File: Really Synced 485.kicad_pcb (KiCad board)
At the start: 2 copper layers, 34 parts, among them J1 CONN_02X04, J2 CONN_01X03, J3 CONN_01X03, J4 CONN_02X04, U1 CE_HEADER, U2 SN75179B, U3 SN65HVD82

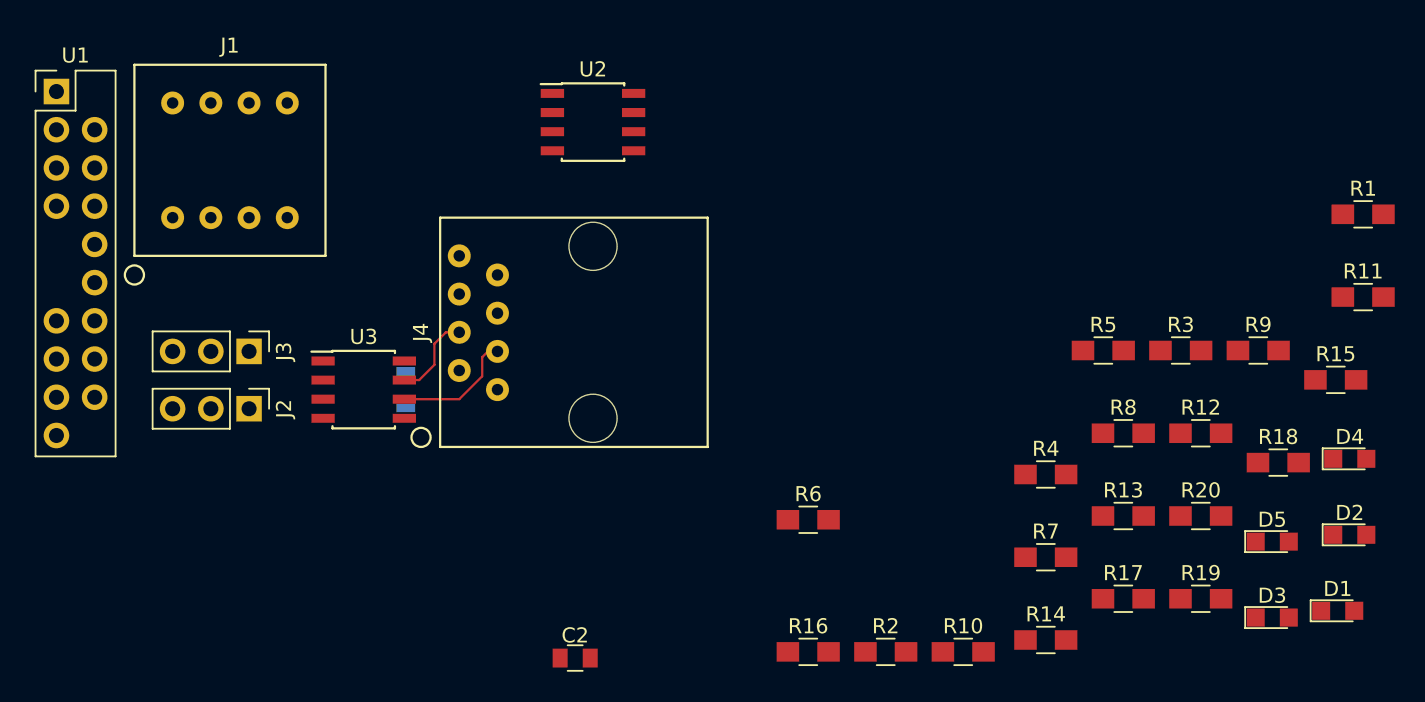
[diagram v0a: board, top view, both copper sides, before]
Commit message: Finished piano switch layout
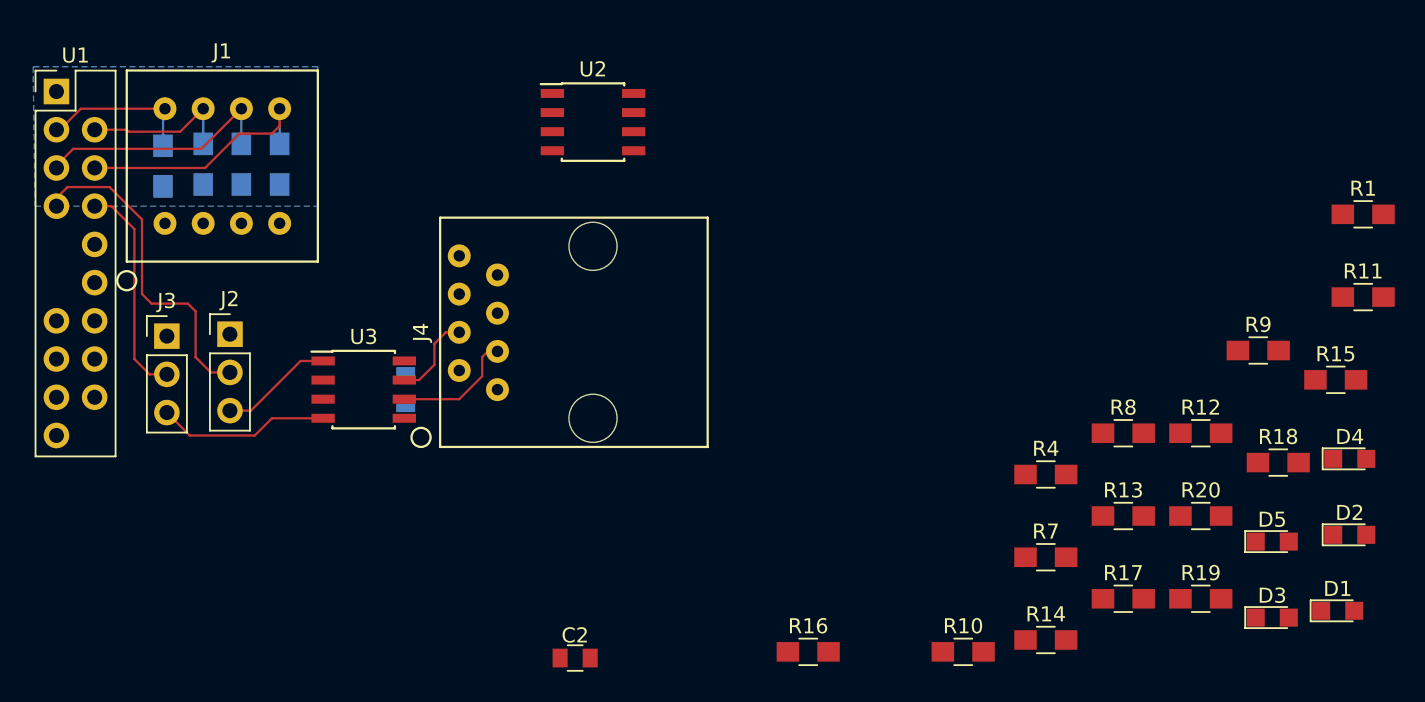
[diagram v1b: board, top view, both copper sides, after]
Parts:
- R2, R3, R5, R6: moved to B.Cu
- moved R3 66.1 mm to (132.8, 109.5), turned to 90 degrees
- moved R5 58.6 mm to (135.4, 109.5), turned to 90 degrees
- moved R2 57.9 mm to (130.2, 109.6), turned to 90 degrees
- moved R6 42.3 mm to (137.9, 109.5), turned to 90 degrees
- moved J3 5.55 mm to (130.4, 120.9), turned to 0 degrees
- moved J2 5.11 mm to (134.6, 120.8), turned to 0 degrees
- moved J1 0.64 mm to (134.1, 109.6)
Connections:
- net Net-(R2-Pad1) renamed /3.3V
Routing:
- net /RX: track 0.00 -> 22.2 mm
- net /ADDR3: track 0.00 -> 16.9 mm
- net /ADDR2: track 0.00 -> 16.3 mm
- net /TX: track 0.00 -> 14.5 mm
- net /TX_HALF: track 0.00 -> 11.5 mm
- net /ADDR0: track 0.00 -> 10.3 mm
- net /ADDR1: track 0.00 -> 10.2 mm
- net /RX_HALF: track 0.00 -> 7.56 mm
- added copper zone on B.Cu, net /3.3V

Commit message: Added ground plane and 5V power routing
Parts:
- C2, R1, R19, R20, R8, R9: moved to B.Cu
- moved D2 69.7 mm to (141.1, 118.7), turned to 90 degrees
- moved D1 68.4 mm to (143.0, 118.7), turned to 90 degrees
- moved D3 68.1 mm to (139.1, 118.7), turned to 90 degrees
- moved R1 67.2 mm to (143.0, 118.5), turned to 90 degrees
- moved D4 64.8 mm to (145.0, 118.7), turned to 90 degrees
- moved D5 59.1 mm to (146.9, 118.7), turned to 90 degrees
- moved R9 56.3 mm to (146.8, 118.5), turned to 90 degrees
- moved R20 51.2 mm to (148.3, 126.4), turned to 90 degrees
- moved R8 49.9 mm to (144.9, 118.5), turned to 90 degrees
- moved R11 46.9 mm to (163.7, 110.2)
- moved R19 46.2 mm to (154.6, 126.4), turned to 90 degrees
- moved C2 21.3 mm to (146.2, 124.3), turned to 90 degrees
- moved C1 17.3 mm to (145.8, 107.2), turned to 270 degrees
- moved U2 10.5 mm to (148.3, 107.8)
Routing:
- net +5V: track 0.00 -> 45.6 mm, vias 0 -> 1
- net /A: track 0.00 -> 13.8 mm
- net /Z: track 0.00 -> 12.3 mm
- net /Y: track 0.00 -> 11.9 mm
- net /B: track 0.00 -> 11.6 mm
- net Net-(J4-Pad1): track 0.00 -> 2.39 mm
- added copper zone on B.Cu, net GND

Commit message: LED placements done
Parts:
- R4, R7: moved to B.Cu
- moved R7 52.5 mm to (139.2, 118.5), turned to 270 degrees
- moved R4 49.1 mm to (141.1, 118.5), turned to 270 degrees
- moved D2 0.13 mm to (141.0, 118.7), turned to 270 degrees
- moved D4 0.13 mm to (144.9, 118.7), turned to 270 degrees
- moved D5 0.13 mm to (146.8, 118.7), turned to 270 degrees
- turned D1 to 270 degrees
- turned D3 to 270 degrees
- turned R1 to 270 degrees
- turned R8 to 270 degrees
- turned R9 to 270 degrees
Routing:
- net Net-(D5-Pad2): track 0.00 -> 35.0 mm
- net /~RX_EN: track 0.00 -> 31.0 mm
- net Net-(D4-Pad2): track 0.00 -> 28.9 mm
- net /TX_EN: track 0.00 -> 26.4 mm
- net Net-(J4-Pad2): track 0.18 -> 2.72 mm
- net +5V: track 45.6 -> 44.0 mm, vias 1 -> 0

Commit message: Finished initial layout, doing DRC next
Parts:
- R10, R11, R13, R14, R16, R17, R18: moved to B.Cu
- moved R15 52.8 mm to (157.3, 109.7)
- moved R14 51.8 mm to (150.8, 105.9), turned to 90 degrees
- moved R13 47.8 mm to (154.6, 105.7), turned to 90 degrees
- moved R18 47.2 mm to (158.5, 117.8)
- moved R12 44.7 mm to (157.3, 111.8)
- moved R10 42.9 mm to (151.3, 113.4)
- moved R17 40.4 mm to (156.9, 122.2), turned to 90 degrees
- moved R16 24.3 mm to (158.8, 122.2), turned to 270 degrees
- moved R11 11.7 mm to (154.8, 117.9), turned to 90 degrees
- moved D2 2.03 mm to (143.0, 118.7)
- moved D1 1.91 mm to (141.1, 118.7)
- moved R1 1.91 mm to (141.1, 118.5)
- moved R4 1.91 mm to (143.0, 118.5)
- moved D3 0.13 mm to (139.2, 118.7)
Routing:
- net +5V: track 44.0 -> 90.7 mm, vias 0 -> 4
- net /RX_FULL: track 0.00 -> 21.8 mm
- net /TX_FULL: track 0.00 -> 20.9 mm
- net /TX: track 14.5 -> 30.1 mm
- net /Y: track 11.9 -> 27.4 mm
- net /Z: track 12.3 -> 22.7 mm, vias 0 -> 1
- net /B_HALF: track 5.78 -> 16.1 mm
- net /RX: track 22.2 -> 30.8 mm
- net /A_HALF: track 8.76 -> 15.9 mm
- net /A: track 13.8 -> 19.9 mm
- net /B: track 11.6 -> 17.4 mm, vias 0 -> 1
- net Net-(D3-Pad1): track 0.00 -> 4.17 mm, vias 0 -> 1
- net Net-(D1-Pad1): track 0.00 -> 3.94 mm, vias 0 -> 1
- net Net-(D5-Pad1): track 0.00 -> 3.87 mm, vias 0 -> 1
- net Net-(D2-Pad1): track 0.00 -> 3.86 mm, vias 0 -> 1
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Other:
- board outline added: 45.1 x 26.2 mm

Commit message: Finished layout with all silkscreen
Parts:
- moved R20 1.52 mm to (149.9, 126.4)
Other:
- board text added: "FULL"
- board text added: "HALF"
- board text added: "PWR"
- board text added: "RX"
- board text added: "STAT1"
- board text added: "STAT2"
- board text added: "TX"
